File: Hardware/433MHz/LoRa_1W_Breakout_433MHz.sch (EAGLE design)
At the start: 26 parts, among them U4 E19-915M30S

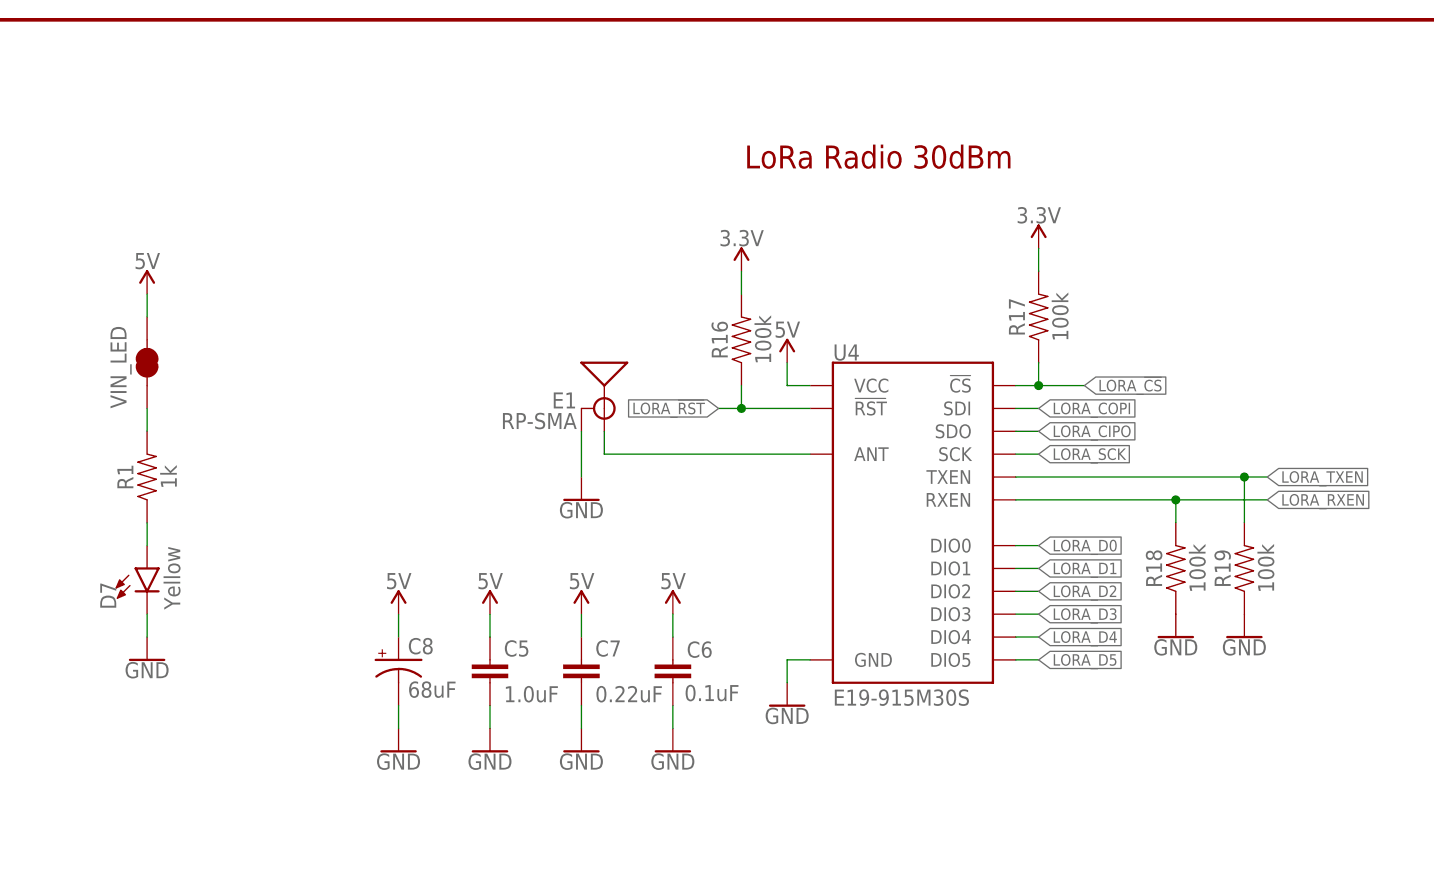
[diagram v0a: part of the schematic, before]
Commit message: Add 433 and 868
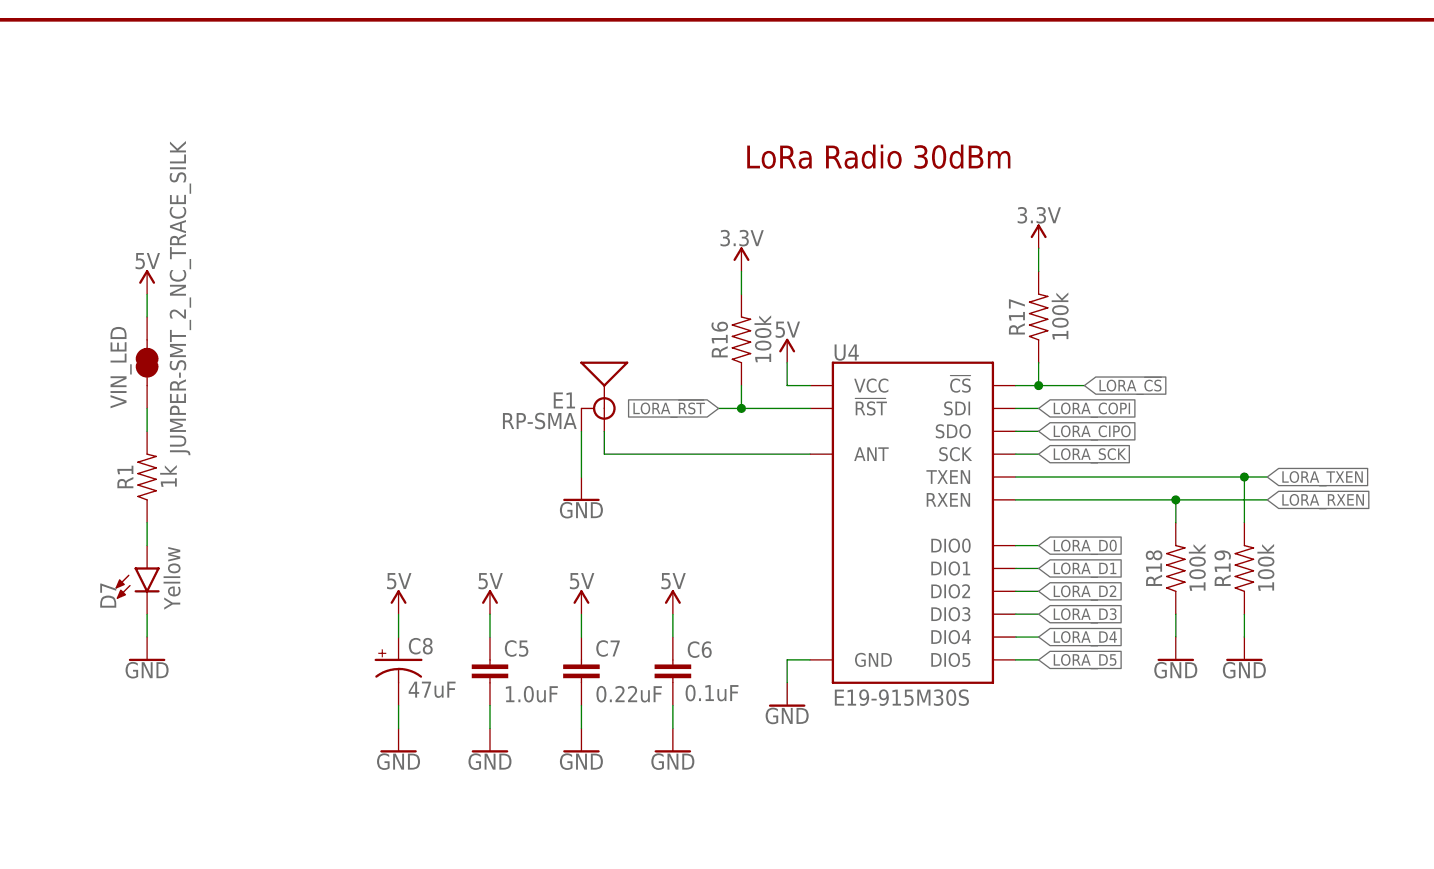
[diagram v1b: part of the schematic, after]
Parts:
- C8: value 68uF -> 47uF; device SparkFun-Capacitors:68UF-POLAR-EIA3528-10V-10%(TANT) -> SparkFun-Capacitors:47UF-POLAR-EIA3528-10V-10%
- E1: device SparkFun-RF:ANTENNA-SMA-GROUNDEDEDGE_RPSMA_SMD -> SparkFun-RF:ANTENNA-SMA-GROUNDEDEDGE_RPSMA
- U4: device SparkFun-RF:E19-915MS1W -> SparkFun-RF:LORA-E19433MHZ

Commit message: Update schematics
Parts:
- U4: value E19-915M30S -> E19-433M30S
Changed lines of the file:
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@@
 <part name="GND16" library="SparkFun-PowerSymbols" deviceset="GND" device=""/>
 <part name="GND24" library="SparkFun-PowerSymbols" deviceset="GND" device=""/>
-<part name="VIN_LED" library="SparkFun-Jumpers" deviceset="JUMPER-SMT_2_NC_TRACE" device="_SILK" package3d_urn="urn:adsk.eagle:package:39281/1" value="JUMPER-SMT_2_NC_TRACE_SILK"/>
+<part name="VIN_LED" library="SparkFun-Jumpers" deviceset="JUMPER-SMT_2_NC_TRACE" device="_SILK" package3d_urn="urn:adsk.eagle:package:39281/1" value=""/>
 <part name="D7" library="SparkFun-LED" deviceset="LED-YELLOW" device="0603" value="Yellow"/>
 <part name="GND28" library="SparkFun-PowerSymbols" deviceset="GND" device=""/>
 <part name="SUPPLY8" library="SparkFun-PowerSymbols" deviceset="5V" device=""/>
 <part name="GND31" library="SparkFun-PowerSymbols" deviceset="GND" device=""/>
-<part name="U4" library="SparkFun-RF" deviceset="LORA-E19" device="433MHZ" value="E19-915M30S"/>
+<part name="U4" library="SparkFun-RF" deviceset="LORA-E19" device="433MHZ" value="E19-433M30S"/>
 <part name="R16" library="SparkFun-Resistors" deviceset="100KOHM" device="-0603-1/10W-1%" value="100k"/>
 <part name="SUPPLY12" library="SparkFun-PowerSymbols" deviceset="3.3V" device=""/>
